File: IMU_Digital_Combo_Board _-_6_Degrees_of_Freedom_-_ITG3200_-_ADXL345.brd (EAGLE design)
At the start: 15.2 x 16.5 mm, 15 parts, among them U1 ADXL345, U3 ITG-32001:1

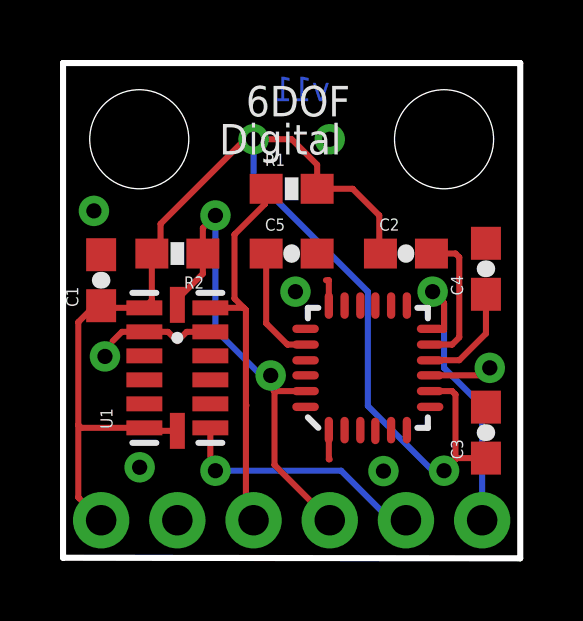
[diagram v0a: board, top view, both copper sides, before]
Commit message: Added production fiducials
Added:
- production fiducials
- flags in schematic for net labels
- modified two traces for better signal integrity
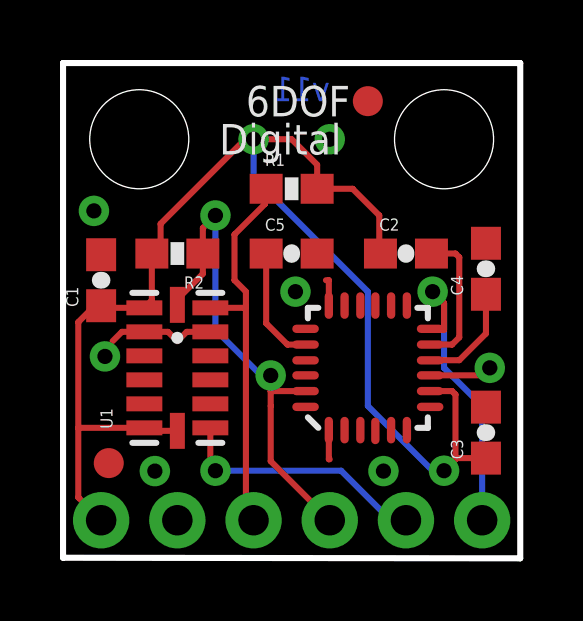
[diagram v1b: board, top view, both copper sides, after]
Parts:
- added JP4, JP6: FIDUCIAL1X2, SparkFun:FIDUCIAL-1X2
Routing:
- net 3.3V: track 45.6 -> 46.1 mm
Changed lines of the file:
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@@
 <element name="U$2" library="SparkFun" package="OSHW-LOGO-S" value="OSHW-LOGOS" x="2.54" y="8.89" rot="MR0"/>
 <element name="U3" library="Testing" package="QFN-24_ITG3200_1:1" value="ITG-32001:1" x="10.16" y="6.35" rot="R90"/>
+<element name="JP4" library="SparkFun" package="FIDUCIAL-1X2" value="FIDUCIAL1X2" x="10.16" y="15.24"/>
+<element name="JP6" library="SparkFun" package="FIDUCIAL-1X2" value="FIDUCIAL1X2" x="1.524" y="3.175"/>
 </elements>
 <signals>
@@
 <via x="1.0287" y="11.5824" extent="1-16" drill="0.508"/>
 <via x="10.6807" y="2.9083" extent="1-16" drill="0.508"/>
-<via x="2.5527" y="3.0353" extent="1-16" drill="0.508"/>
+<via x="3.0607" y="2.9083" extent="1-16" drill="0.508"/>
 <polygon width="0.2032" layer="16" isolate="0.3048">
 <vertex x="15.24" y="16.51"/>
@@
 <wire x1="2.81" y1="4.25" x2="3.81" y2="4.25" width="0.2032" layer="1"/>
 <wire x1="2.71" y1="4.35" x2="2.81" y2="4.25" width="0.2032" layer="1"/>
-<wire x1="0.508" y1="4.445" x2="0.508" y2="2.032" width="0.2032" layer="1"/>
-<wire x1="0.603" y1="4.35" x2="2.71" y2="4.35" width="0.2032" layer="1"/>
-<wire x1="0.508" y1="4.445" x2="0.603" y2="4.35" width="0.2032" layer="1"/>
 <wire x1="0.984" y1="8.35" x2="1.27" y2="8.35" width="0.2032" layer="1"/>
 <wire x1="1.27" y1="8.35" x2="2.71" y2="8.35" width="0.2032" layer="1"/>
 <wire x1="0.984" y1="8.35" x2="0.508" y2="7.874" width="0.2032" layer="1"/>
-<wire x1="0.508" y1="7.874" x2="0.508" y2="4.445" width="0.2032" layer="1"/>
+<wire x1="0.508" y1="7.874" x2="0.508" y2="4.35" width="0.2032" layer="1"/>
+<wire x1="0.508" y1="4.35" x2="0.508" y2="2.032" width="0.2032" layer="1"/>
 <wire x1="2.96" y1="10.16" x2="3.16" y2="10.3355" width="0.2032" layer="1"/>
 <wire x1="3.16" y1="10.3355" x2="3.2512" y2="10.4267" width="0.2032" layer="1"/>
@@
 <wire x1="12.2362" y1="5.5746" x2="12.9674" y2="5.5746" width="0.2032" layer="1"/>
 <wire x1="12.9674" y1="5.5746" x2="13.081" y2="5.461" width="0.2032" layer="1"/>
-<wire x1="13.081" y1="5.461" x2="13.081" y2="3.341" width="0.2032" layer="1"/>
-<wire x1="13.081" y1="3.341" x2="13.081" y2="3.302" width="0.2032" layer="1"/>
+<wire x1="13.081" y1="5.461" x2="13.081" y2="3.302" width="0.2032" layer="1"/>
 <wire x1="13.081" y1="3.302" x2="12.7" y2="2.921" width="0.2032" layer="1"/>
 <via x="12.7" y="2.921" extent="1-16" drill="0.508"/>
 <wire x1="12.7" y1="2.921" x2="12.319" y2="2.921" width="0.2032" layer="16"/>
 <wire x1="12.319" y1="2.921" x2="10.16" y2="5.08" width="0.2032" layer="16"/>
-<wire x1="14.097" y1="3.341" x2="13.081" y2="3.341" width="0.2032" layer="1"/>
 <wire x1="10.16" y1="5.08" x2="10.16" y2="8.89" width="0.2032" layer="16"/>
 <wire x1="10.16" y1="8.89" x2="6.35" y2="12.7" width="0.2032" layer="16"/>
@@
 <via x="6.35" y="13.97" extent="1-16" drill="0.508"/>
 <wire x1="6.35" y1="13.97" x2="7.62" y2="13.97" width="0.2032" layer="1"/>
+<wire x1="2.71" y1="4.35" x2="0.508" y2="4.35" width="0.2032" layer="1"/>
+<wire x1="14.097" y1="3.341" x2="13.12" y2="3.341" width="0.2032" layer="1"/>
+<wire x1="13.12" y1="3.341" x2="12.7" y2="2.921" width="0.2032" layer="1"/>
 </signal>
 <signal name="SCL">
 <contactref element="U1" pad="14"/>
 <contactref element="JP1" pad="4"/>
-<wire x1="7.0485" y1="3.1115" x2="8.89" y2="1.27" width="0.2032" layer="1"/>
 <wire x1="5.08" y1="7.62" x2="6.604" y2="6.096" width="0.2032" layer="16"/>
 <wire x1="5.08" y1="11.43" x2="5.08" y2="7.62" width="0.2032" layer="16"/>
@@
 <contactref element="U3" pad="23"/>
 <wire x1="4.66" y1="11.01" x2="4.66" y2="10.16" width="0.2032" layer="1"/>
-<wire x1="7.0485" y1="5.5746" x2="7.0485" y2="3.1115" width="0.2032" layer="1"/>
-<wire x1="8.0838" y1="5.5746" x2="7.0485" y2="5.5746" width="0.2032" layer="1"/>
 <wire x1="3.81" y1="8.45" x2="3.81" y2="8.636" width="0.2032" layer="1"/>
 <wire x1="3.81" y1="8.636" x2="4.66" y2="9.486" width="0.2032" layer="1"/>
 <wire x1="4.66" y1="9.486" x2="4.66" y2="10.16" width="0.2032" layer="1"/>
-<wire x1="7.0485" y1="5.5746" x2="6.9215" y2="5.7016" width="0.2032" layer="1"/>
-<wire x1="6.9215" y1="5.7016" x2="6.9215" y2="6.096" width="0.2032" layer="1"/>
 <wire x1="6.604" y1="6.096" x2="6.9215" y2="6.096" width="0.2032" layer="16"/>
+<wire x1="6.9215" y1="6.096" x2="6.9215" y2="5.5746" width="0.2032" layer="1"/>
+<wire x1="6.9215" y1="5.08" x2="6.9215" y2="3.2385" width="0.2032" layer="1"/>
+<wire x1="6.9215" y1="3.2385" x2="8.89" y2="1.27" width="0.2032" layer="1"/>
+<wire x1="8.0838" y1="5.5746" x2="6.9215" y2="5.5746" width="0.2032" layer="1"/>
+<wire x1="6.9215" y1="5.5746" x2="6.9215" y2="5.08" width="0.2032" layer="1"/>
 </signal>
 <signal name="SDA">
@@
 <contactref element="R1" pad="1"/>
 <contactref element="JP1" pad="3"/>
-<wire x1="5.175" y1="8.35" x2="4.91" y2="8.35" width="0.2032" layer="1"/>
-<wire x1="5.175" y1="8.35" x2="5.207" y2="8.382" width="0.2032" layer="1"/>
-<wire x1="6.096" y1="5.08" x2="6.096" y2="1.524" width="0.2032" layer="1"/>
-<wire x1="6.0259" y1="8.35" x2="5.175" y2="8.35" width="0.2032" layer="1"/>
-<wire x1="6.096" y1="5.08" x2="6.116" y2="5.1" width="0.2032" layer="1"/>
-<wire x1="6.096" y1="1.524" x2="6.35" y2="1.27" width="0.2032" layer="1"/>
-<wire x1="6.096" y1="5.08" x2="6.096" y2="8.2799" width="0.2032" layer="1"/>
-<wire x1="6.096" y1="8.2799" x2="6.0259" y2="8.35" width="0.2032" layer="1"/>
-<wire x1="6.0259" y1="8.35" x2="5.715" y2="8.6609" width="0.2032" layer="1"/>
-<wire x1="5.715" y1="8.6609" x2="5.715" y2="10.795" width="0.2032" layer="1"/>
 <wire x1="6.77" y1="12.319" x2="6.731" y2="12.319" width="0.2032" layer="1"/>
 <wire x1="5.715" y1="10.795" x2="6.731" y2="11.811" width="0.2032" layer="1"/>
 <wire x1="6.731" y1="12.319" x2="6.731" y2="11.811" width="0.2032" layer="1"/>
+<wire x1="5.715" y1="10.795" x2="5.715" y2="9.271" width="0.2032" layer="1"/>
+<wire x1="5.715" y1="9.271" x2="6.096" y2="8.89" width="0.2032" layer="1"/>
+<wire x1="6.096" y1="8.89" x2="6.096" y2="8.382" width="0.2032" layer="1"/>
+<wire x1="6.096" y1="8.382" x2="6.096" y2="1.524" width="0.2032" layer="1"/>
+<wire x1="6.096" y1="1.524" x2="6.35" y2="1.27" width="0.2032" layer="1"/>
+<wire x1="4.91" y1="8.35" x2="6.064" y2="8.35" width="0.2032" layer="1"/>
+<wire x1="6.064" y1="8.35" x2="6.096" y2="8.382" width="0.2032" layer="1"/>
 </signal>
 <signal name="INT1">
@@
 </signal>
 </signals>
+<errors>
+</errors>
 </board>
 </drawing>
